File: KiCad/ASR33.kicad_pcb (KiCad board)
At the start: 2 copper layers, 42 x 35 mm, 36 parts, among them J1 USB-C, J2 Conn_01x04, J3 Conn_01x05, Q1 NX7002AK, SW1 SW_Push, U1 ESP32-WROOM-32, U2 FT231XQ, U3 NCR402U, U4 NCR402U, U5 LMR16006+FB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

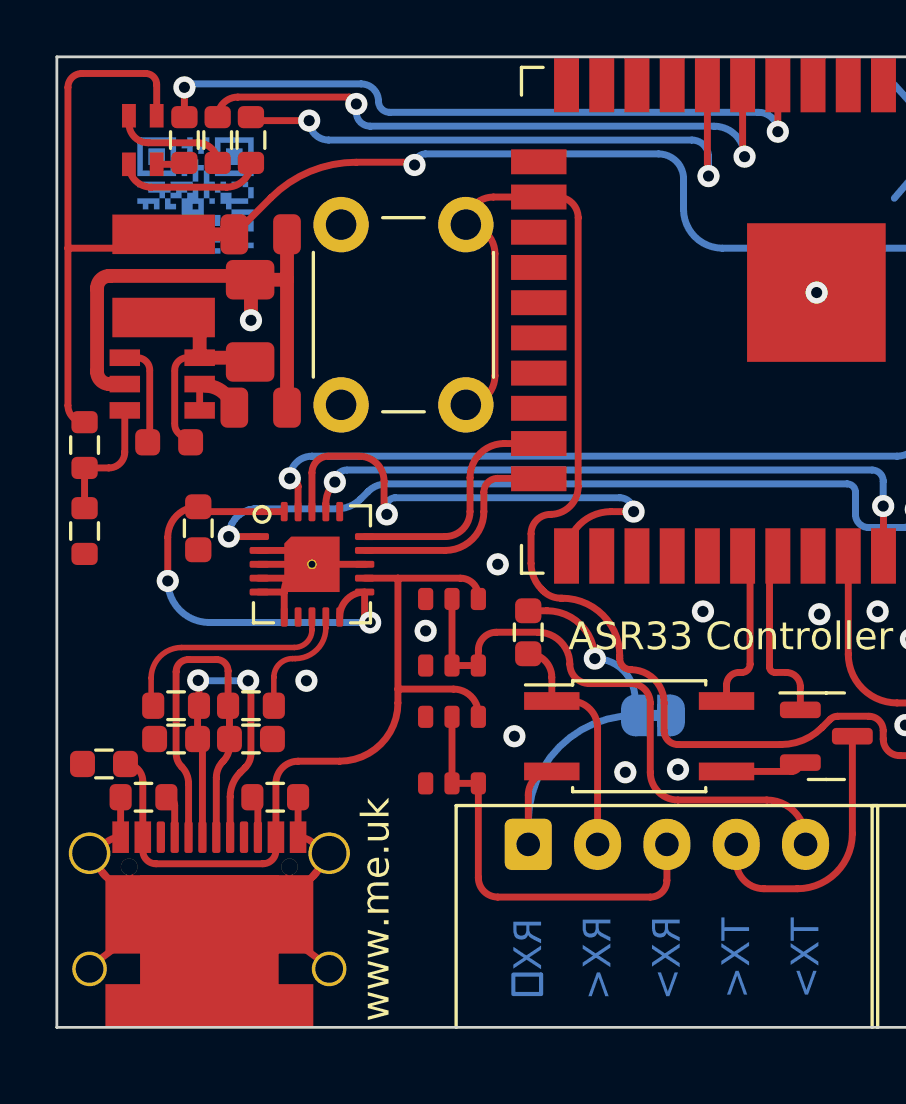
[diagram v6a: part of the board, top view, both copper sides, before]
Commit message: Added network on Tx, same as FS-2 send circuit.
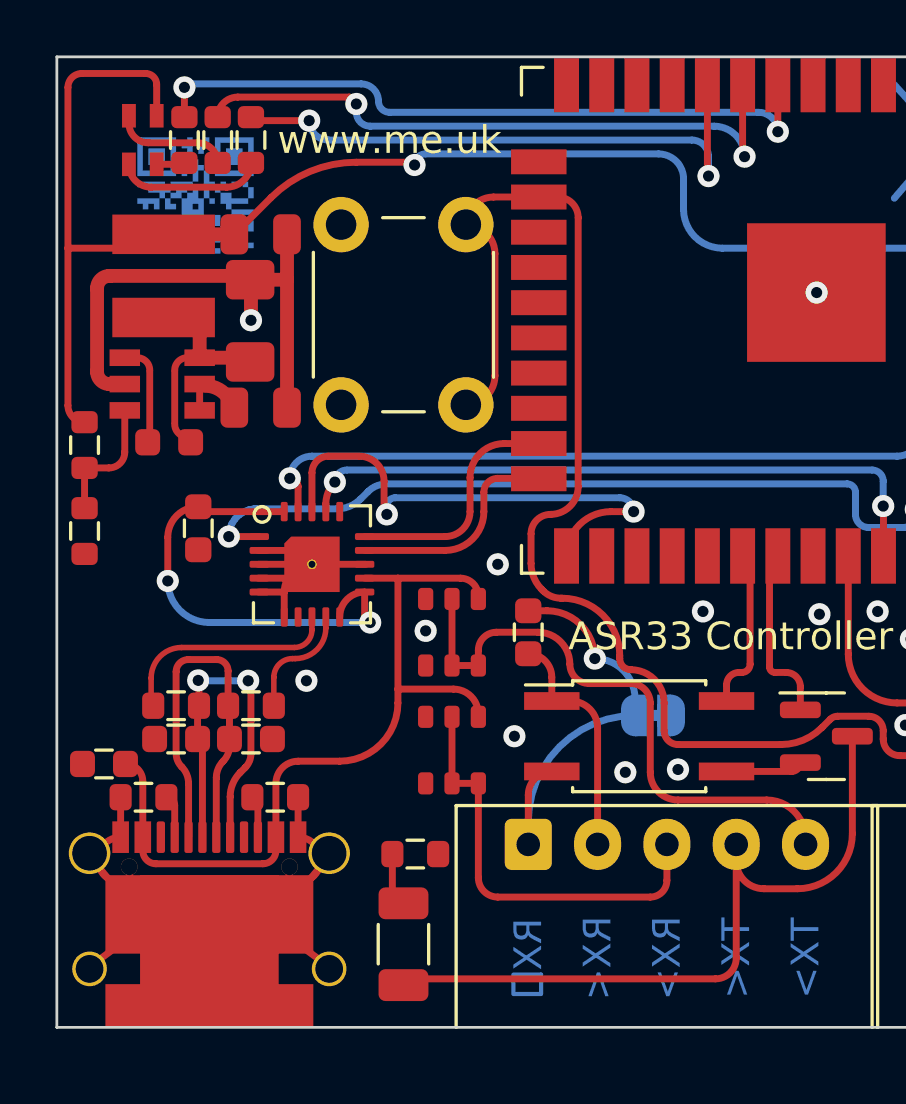
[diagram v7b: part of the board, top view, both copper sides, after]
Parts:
- added C5: 110nF, Capacitor_SMD:C_1206_3216Metric, F.Cu at (130.5, 140.0)
- added R10: 470R, RevK:R_0603, F.Cu at (130.9, 136.8)
- renumbered C5 to C6, C6 to C7, C7 to C8, C8 to C9
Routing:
- net Net-(C5-Pad1): track 9.89 -> 26.5 mm
- net Net-(C5-Pad2): track 0.00 -> 1.99 mm

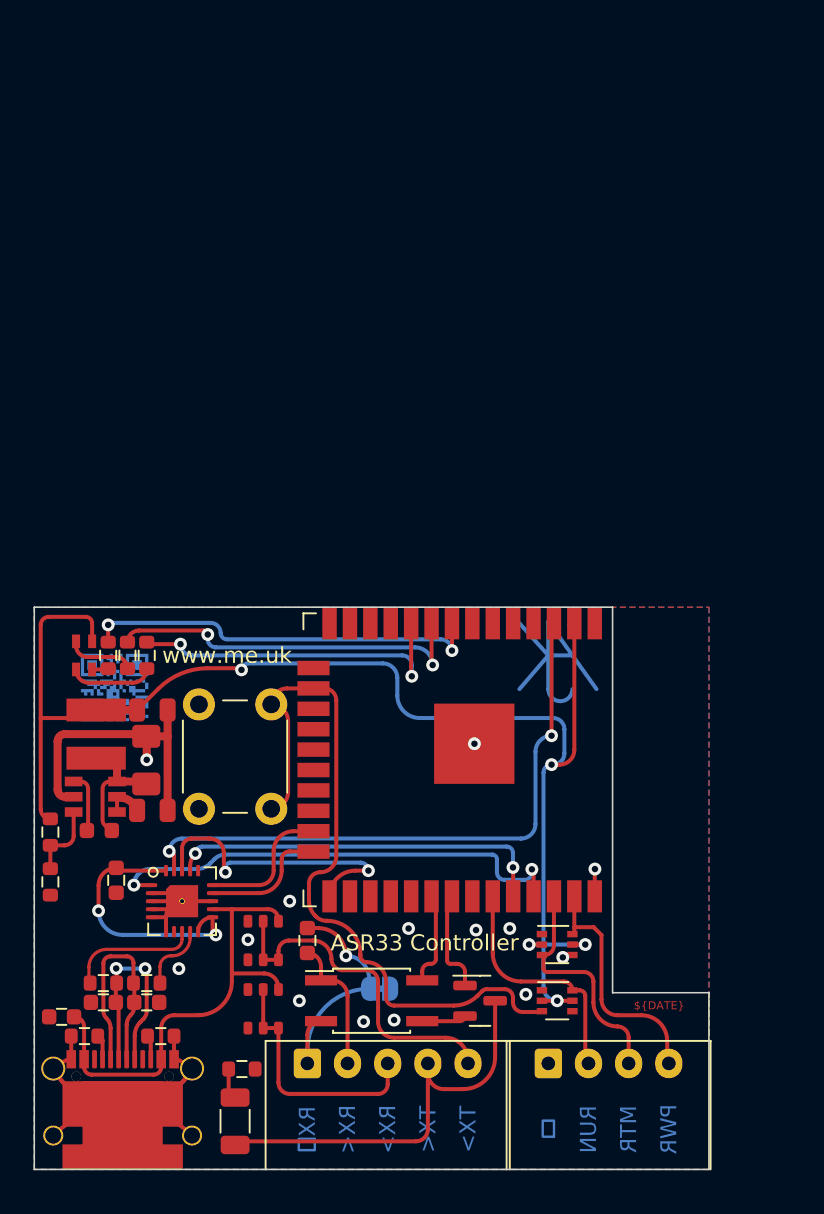
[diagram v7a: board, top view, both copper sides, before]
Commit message: Complete re-work with more connectors.
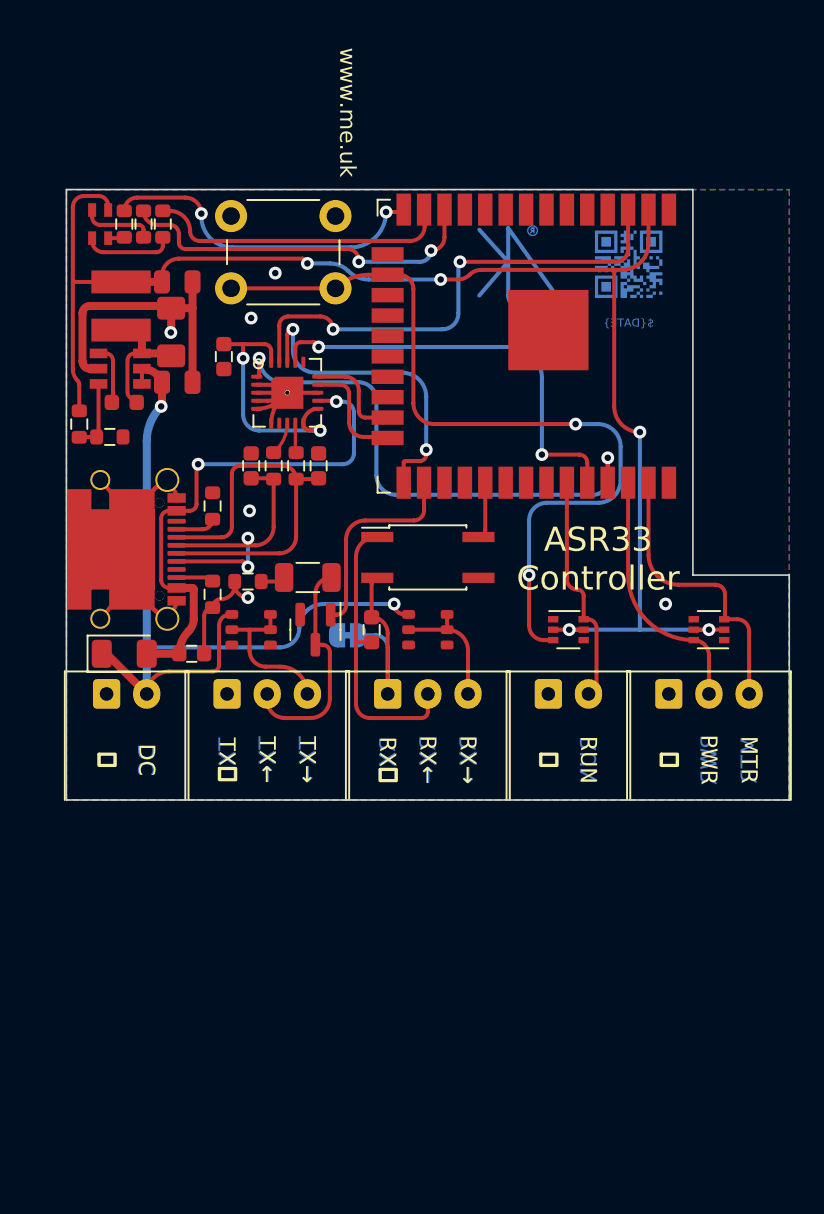
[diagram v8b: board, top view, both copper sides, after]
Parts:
- added D4: D, Diode_SMD:D_1206_3216Metric, F.Cu at (123.6, 110.9)
- added J4: RUN, RevK:Molex_MiniSPOX_H2RA, F.Cu at (151.2, 113.4)
- added J5: Tx, RevK:Molex_MiniSPOX_H3RA, F.Cu at (132.5, 113.4)
- added J6: Rx, RevK:Molex_MiniSPOX_H3RA, F.Cu at (142.5, 113.4)
- C5: value 110nF -> 110nF NF
- C6: renamed from C9; value NF -> 10nF NF
- J2: value Conn_01x04 -> DC; footprint RevK:Molex_MiniSPOX_H4RA -> RevK:Molex_MiniSPOX_H2RA
- J3: value Conn_01x05 -> Power; footprint RevK:Molex_MiniSPOX_H5RA -> RevK:Molex_MiniSPOX_H3RA
- R1: value 732R -> 1K
- R10: value 470R -> 470R NF
- R3: value 324R -> 470R
- moved U7 41.5 mm to (155.0, 86.7)
- moved J1 38.8 mm to (120.0, 104.4), turned to -90 degrees
- moved J2 37.8 mm to (123.8, 113.4)
- moved C2 35.1 mm to (135.7, 99.2), turned to 90 degrees
- moved C3 34.6 mm to (131.5, 99.2), turned to 90 degrees
- moved C5 34.2 mm to (135.0, 106.2), turned to 180 degrees
- moved R4 33.9 mm to (129.1, 101.7), turned to 90 degrees
- moved R7 33.9 mm to (132.9, 99.2), turned to -90 degrees
- moved R6 33.5 mm to (134.3, 99.2), turned to 90 degrees
- moved C1 33.3 mm to (129.8, 92.4)
- moved U2 32.3 mm to (133.8, 94.7)
- moved SW1 31.5 mm to (133.5, 85.9), turned to 0 degrees
- moved J3 30.5 mm to (160.0, 113.4)
- moved R10 30.4 mm to (131.3, 106.4), turned to 180 degrees
- moved R9 27.9 mm to (122.7, 97.4), turned to 180 degrees
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- renumbered C6 to C7, C7 to C8, C8 to C9, D4 to D5, U6 to U5, U5 to U6
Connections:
- C6 pad 1: Net-(C9-Pad1) -> Net-(C6-Pad1)
- C6 pad 2: Net-(C9-Pad2) -> Net-(C6-Pad2)
- J2 pad 2: RUN -> DC
- J3 pad 1: Net-(C9-Pad1) -> GND
- J3 pad 2: Net-(C9-Pad2) -> PWR
- J3 pad 3: Net-(J3-Pad3) -> MTR
- JP1 pad 2: Net-(C9-Pad1) -> Net-(C6-Pad1)
- U1 pad 10: G -> unconnected-(U1-Pad10)
- U1 pad 12: unconnected-(U1-Pad12) -> B
- U1 pad 13: unconnected-(U1-Pad13) -> G
- U1 pad 14: unconnected-(U1-Pad14) -> R
- U1 pad 26: unconnected-(U1-Pad26) -> TX20MA
- U1 pad 29: unconnected-(U1-Pad29) -> RX20MA
- U1 pad 30: RX20MA -> unconnected-(U1-Pad30)
- U1 pad 31: TX20MA -> unconnected-(U1-Pad31)
- U1 pad 36: MTR -> PWR
- U1 pad 37: PWR -> MTR
- U1 pad 8: R -> unconnected-(U1-Pad8)
- U1 pad 9: B -> unconnected-(U1-Pad9)
- U3 pad 2: Net-(J3-Pad5) -> Net-(J5-Pad3)
- U3 pad 3: Net-(J3-Pad5) -> Net-(J5-Pad3)
- U3 pad 4: VBUS -> DC
- U3 pad 5: Net-(J3-Pad5) -> Net-(J5-Pad3)
- U4 pad 2: Net-(J3-Pad3) -> Net-(J6-Pad3)
- U4 pad 3: Net-(J3-Pad3) -> Net-(J6-Pad3)
- U4 pad 4: VBUS -> DC
- U4 pad 5: Net-(J3-Pad3) -> Net-(J6-Pad3)
- U5 pad 1: Net-(C9-Pad2) -> Net-(C6-Pad2)
- U5 pad 2: Net-(C9-Pad1) -> Net-(C6-Pad1)
- U6 pad 1: Net-(U5-Pad1) -> DC
- U6 pad 2: Net-(U5-Pad1) -> DC
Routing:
- net DC: track 0.00 -> 51.6 mm, vias 0 -> 2
- net Net-(J3-Pad5): track 21.4 -> 0.00 mm
- net Net-(C6-Pad2): track 0.00 -> 18.4 mm
- net Net-(C9-Pad1): track 15.9 -> 0.00 mm, vias 1 -> 0
- net Net-(J3-Pad3): track 15.5 -> 0.00 mm
- net Net-(C6-Pad1): track 0.00 -> 13.1 mm
- net Net-(C5-Pad1): track 26.5 -> 14.3 mm
- net Net-(C2-Pad1): track 14.5 -> 24.8 mm
- net Net-(J5-Pad3): track 0.00 -> 9.68 mm
- net Net-(C9-Pad2): track 8.52 -> 0.00 mm
- net Net-(J6-Pad3): track 0.00 -> 8.04 mm
- net EN: track 38.2 -> 31.3 mm
- net TX20MA: track 6.49 -> 12.9 mm
- net D+: track 8.19 -> 2.06 mm
- net BUTTON: track 45.7 -> 51.1 mm, vias 0 -> 2
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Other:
- board size 42 x 35 mm -> 45 x 38 mm
- board text added: "12V"
- board text added: "20mA"
- board text added: "3.3V"
- board text added: "5V"
- board text added: "Alternatives"
- board text added: "DC"
- board text added: "RX←"
- board text added: "RX→"
- board text added: "TX←"
- board text added: "TX→"
- board text added: "TX⏚"
- board text removed: "Control (3.3V)"
- board text removed: "Ext Power"
- board text removed: "RX<"
- board text removed: "RX>"
- board text removed: "TX<"
- board text removed: "TX>"
- board text removed: "Teletype (20mA)"
